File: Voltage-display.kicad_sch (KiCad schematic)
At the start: 17 parts, among them J1 Conn_01x02, J2 Conn_01x02, U1 AMC1311BQDWVQ1, U2 R05CT05S-R

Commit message: Assigned Footprints to the components
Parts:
- U1: footprint DWV8_TEX -> ul_AMC1311BQDWVQ1_footprints:DWV8_TEX
- U2: footprint SMD_16_10.3X7.5X2.6_RCP -> R05CT055_R_footprints:SMD_16_10.3X7.5X2.6_RCP
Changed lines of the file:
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@@
 			)
 		)
-		(property "Footprint" "DWV8_TEX"
+		(property "Footprint" "ul_AMC1311BQDWVQ1_footprints:DWV8_TEX"
 			(at 102.87 125.73 0)
 			(hide yes)
@@
 			)
 		)
-		(property "Footprint" "SMD_16_10.3X7.5X2.6_RCP"
+		(property "Footprint" "R05CT055_R_footprints:SMD_16_10.3X7.5X2.6_RCP"
 			(at 97.79 36.83 0)
 			(hide yes)

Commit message: Assigned more footprints on caps and resistors
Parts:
- C1, C2, C3, C4, C5, C6, C8: footprint (none) -> Capacitor_SMD:C_0805_2012Metric_Pad1.18x1.45mm_HandSolder
- C7, C9: footprint (none) -> Capacitor_SMD:C_1206_3216Metric_Pad1.33x1.80mm_HandSolder
- R1: footprint Resistor_THT:R_Array_SIP6 -> Resistor_SMD:R_1206_3216Metric_Pad1.30x1.75mm_HandSolder
- R2, R3, R4: footprint (none) -> Resistor_SMD:R_1206_3216Metric_Pad1.30x1.75mm_HandSolder
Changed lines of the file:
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@@
 			)
 		)
-		(property "Footprint" ""
+		(property "Footprint" "Capacitor_SMD:C_1206_3216Metric_Pad1.33x1.80mm_HandSolder"
 			(at 187.6552 86.36 0)
 			(hide yes)
@@
 			)
 		)
-		(property "Footprint" ""
+		(property "Footprint" "Capacitor_SMD:C_0805_2012Metric_Pad1.18x1.45mm_HandSolder"
 			(at 171.1452 86.36 0)
 			(hide yes)
@@
 			)
 		)
-		(property "Footprint" ""
+		(property "Footprint" "Resistor_SMD:R_1206_3216Metric_Pad1.30x1.75mm_HandSolder"
 			(at 20.32 44.45 0)
 			(hide yes)
@@
 			)
 		)
-		(property "Footprint" ""
+		(property "Footprint" "Capacitor_SMD:C_0805_2012Metric_Pad1.18x1.45mm_HandSolder"
 			(at 220.6752 34.29 0)
 			(hide yes)
@@
 			)
 		)
-		(property "Footprint" ""
+		(property "Footprint" "Resistor_SMD:R_1206_3216Metric_Pad1.30x1.75mm_HandSolder"
 			(at 20.32 66.04 0)
 			(hide yes)
@@
 			)
 		)
-		(property "Footprint" ""
+		(property "Footprint" "Capacitor_SMD:C_0805_2012Metric_Pad1.18x1.45mm_HandSolder"
 			(at 174.9552 34.29 0)
 			(hide yes)
@@
 			)
 		)
-		(property "Footprint" "Resistor_THT:R_Array_SIP6"
+		(property "Footprint" "Resistor_SMD:R_1206_3216Metric_Pad1.30x1.75mm_HandSolder"
 			(at 20.32 34.29 0)
 			(hide yes)
@@
 			)
 		)
-		(property "Footprint" ""
+		(property "Footprint" "Capacitor_SMD:C_1206_3216Metric_Pad1.33x1.80mm_HandSolder"
 			(at 220.6752 85.09 0)
 			(hide yes)
@@
 			)
 		)
-		(property "Footprint" ""
+		(property "Footprint" "Capacitor_SMD:C_0805_2012Metric_Pad1.18x1.45mm_HandSolder"
 			(at 204.1652 85.09 0)
 			(hide yes)
@@
 			)
 		)
-		(property "Footprint" ""
+		(property "Footprint" "Resistor_SMD:R_1206_3216Metric_Pad1.30x1.75mm_HandSolder"
 			(at 20.32 54.61 0)
 			(hide yes)
@@
 			)
 		)
-		(property "Footprint" ""
+		(property "Footprint" "Capacitor_SMD:C_0805_2012Metric_Pad1.18x1.45mm_HandSolder"
 			(at 36.5252 72.39 0)
 			(hide yes)
@@
 			)
 		)
-		(property "Footprint" ""
+		(property "Footprint" "Capacitor_SMD:C_0805_2012Metric_Pad1.18x1.45mm_HandSolder"
 			(at 191.4652 34.29 0)
 			(hide yes)
@@
 			)
 		)
-		(property "Footprint" ""
+		(property "Footprint" "Capacitor_SMD:C_0805_2012Metric_Pad1.18x1.45mm_HandSolder"
 			(at 204.1652 34.29 0)
 			(hide yes)

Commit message: Add KiCad project
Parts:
- J1, J2: footprint (none) -> Connector:Banana_Jack_2Pin
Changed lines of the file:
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@@
 			)
 		)
-		(property "Footprint" ""
+		(property "Footprint" "Connector:Banana_Jack_2Pin"
 			(at 53.34 27.94 0)
 			(hide yes)
@@
 			)
 		)
-		(property "Footprint" ""
+		(property "Footprint" "Connector:Banana_Jack_2Pin"
 			(at 38.1 114.3 0)
 			(hide yes)

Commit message: Update KiCad PCB
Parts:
- J1, J2: footprint Connector:Banana_Jack_2Pin -> TerminalBlock_Phoenix:TerminalBlock_Phoenix_PTSM-0,5-2-2,5-V-SMD_1x02-1MP_P2.50mm_Vertical
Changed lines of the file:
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@@
 			)
 		)
-		(property "Footprint" "Connector:Banana_Jack_2Pin"
+		(property "Footprint" "TerminalBlock_Phoenix:TerminalBlock_Phoenix_PTSM-0,5-2-2,5-V-SMD_1x02-1MP_P2.50mm_Vertical"
 			(at 53.34 27.94 0)
 			(hide yes)
@@
 			)
 		)
-		(property "Footprint" "Connector:Banana_Jack_2Pin"
+		(property "Footprint" "TerminalBlock_Phoenix:TerminalBlock_Phoenix_PTSM-0,5-2-2,5-V-SMD_1x02-1MP_P2.50mm_Vertical"
 			(at 38.1 114.3 0)
 			(hide yes)

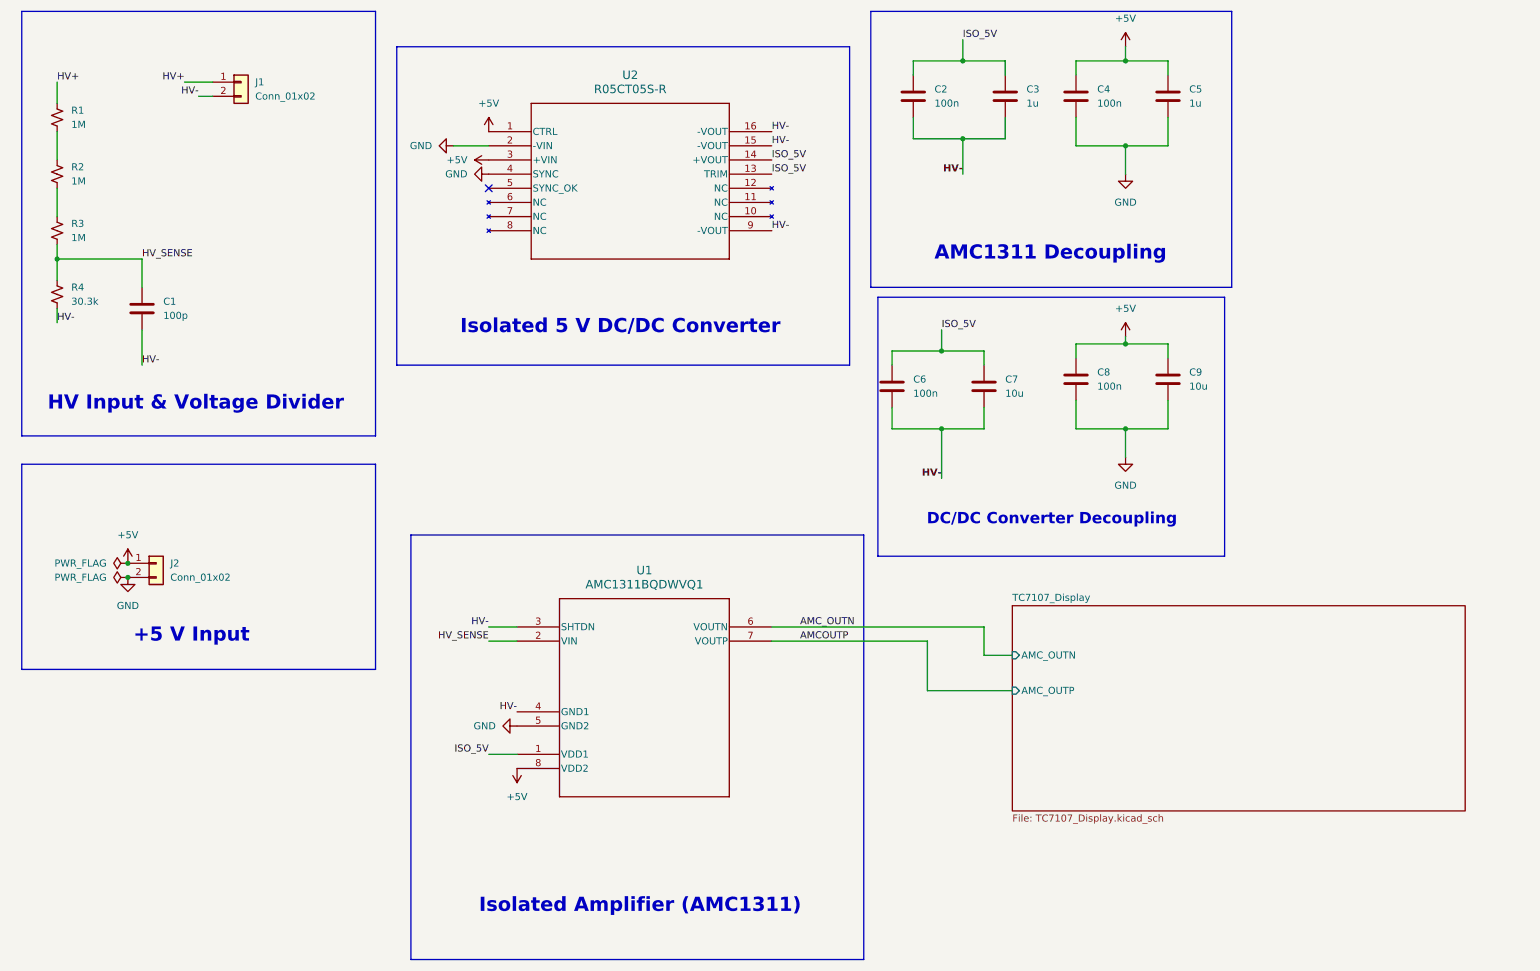
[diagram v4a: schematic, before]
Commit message: Updated with Safety/Protection features
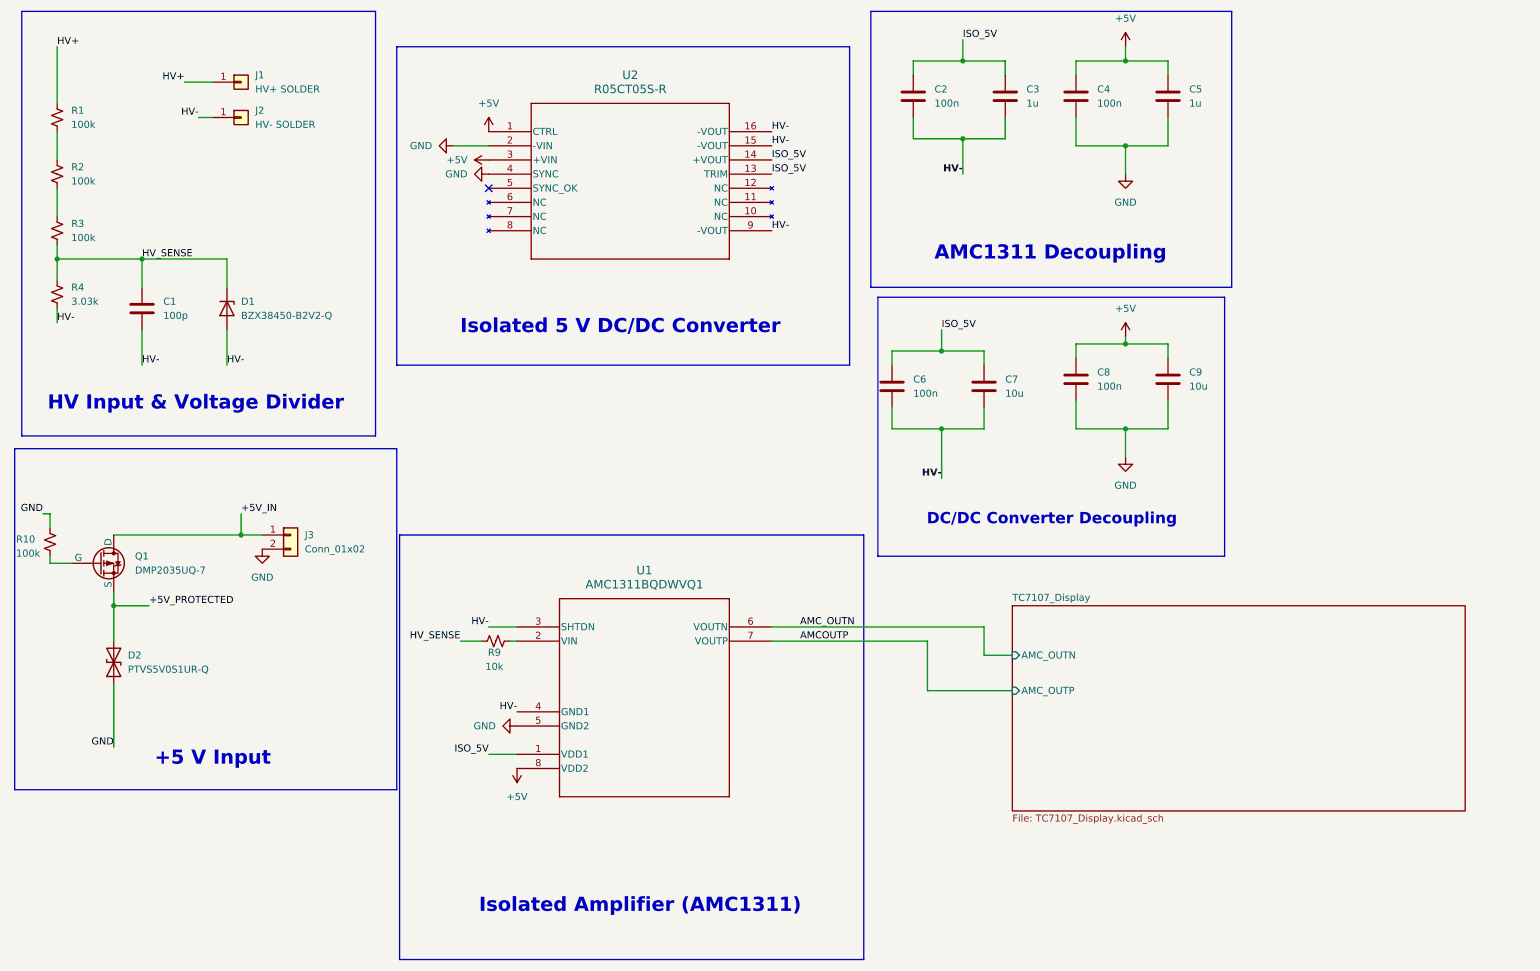
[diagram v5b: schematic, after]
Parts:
- removed J1: Conn_01x02, TerminalBlock_Phoenix:TerminalBlock_Phoenix_PTSM-0,5-2-2,5-V-SMD_1x02-1MP_P2.50mm_Vertical, symbol Connector_Generic:Conn_01x02
- added D1: BZX38450-B2V2-Q, Diode_SMD:D_SOD-323_HandSoldering, symbol Device:D_Zener
- added D2: PTVS5V0S1UR-Q, Voltage_Display_Footprints:SOD123W, symbol Device:D_TVS
- added J1: HV+ SOLDER, Connector_Wire:SolderWire-0.5sqmm_1x01_D0.9mm_OD2.1mm_Relief, symbol Connector_Generic:Conn_01x01
- added J2: HV- SOLDER, Connector_Wire:SolderWire-0.5sqmm_1x01_D0.9mm_OD2.1mm_Relief, symbol Connector_Generic:Conn_01x01
- added Q1: DMP2035UQ-7, Voltage_Display_Footprints:SOT96P240X115-3N, symbol Simulation_SPICE:PMOS
- added R10: 100k, Resistor_SMD:R_1206_3216Metric_Pad1.30x1.75mm_HandSolder, symbol Device:R_Small_US
- added R9: 10k, Resistor_SMD:R_1206_3216Metric_Pad1.30x1.75mm_HandSolder, symbol Device:R_Small_US
- J3: renamed from J2; footprint TerminalBlock_Phoenix:TerminalBlock_Phoenix_PTSM-0,5-2-2,5-V-SMD_1x02-1MP_P2.50mm_Vertical -> Connector_PinHeader_2.54mm:PinHeader_1x02_P2.54mm_Vertical
- R1, R2, R3: value 1M -> 100k
- R4: value 30.3k -> 3.03k
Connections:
- net +5V: no longer J3.1 (Pin_1)
- net GND: now also D2.1 (A1), R10.1
- net HV+: now also J1.1 (Pin_1)
- net HV-: now also D1.2 (A), J2.1 (Pin_1)
- net HV_SENSE: now also D1.1 (K), R9.1; no longer U1.2 (VIN)
- new net: R9.2, U1.2 (VIN)
- new net: Q1.2 (G), R10.2
- new net +5V_IN: J3.1 (Pin_1), Q1.1 (D)
- new net +5V_PROTECTED: D2.2 (A2), Q1.3 (S)
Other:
- moved on the sheet: J3

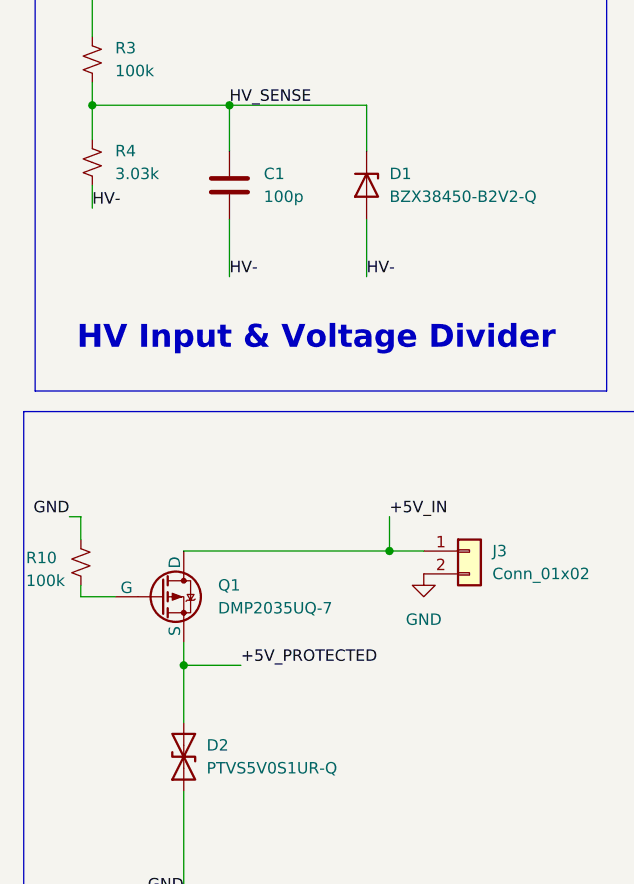
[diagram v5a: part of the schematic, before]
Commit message: Added the switch for the votlage display
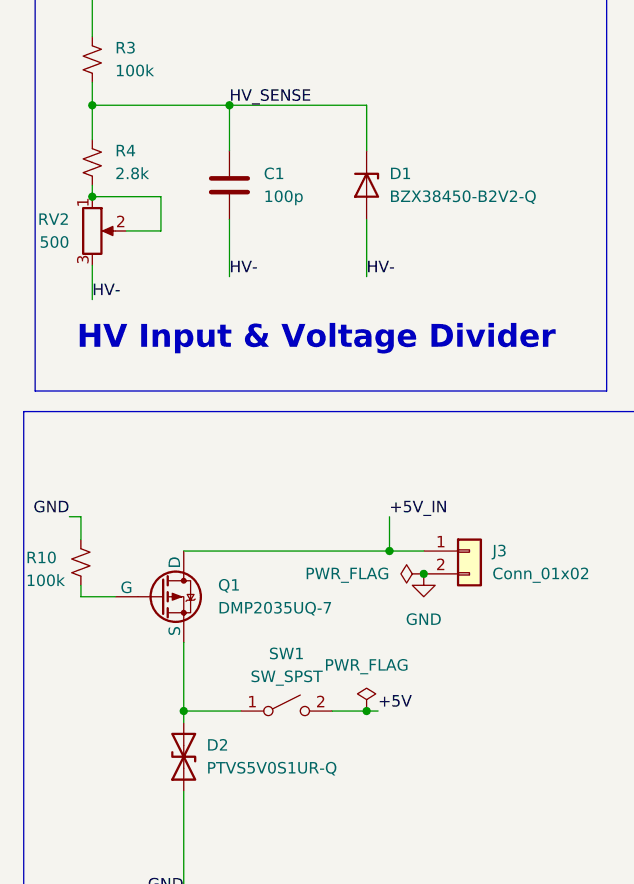
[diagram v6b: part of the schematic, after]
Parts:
- added RV2: 500, Potentiometer_THT:Potentiometer_Bourns_3296W_Vertical, symbol Device:R_Potentiometer
- added SW1: SW_SPST, symbol Switch:SW_SPST
- R4: value 3.03k -> 2.8k
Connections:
- net +5V: now also SW1.2 (B)
- net HV-: now also RV2.3; no longer R4.2
- net +5V_PROTECTED: no longer names the net of D2.2 (A2), Q1.3 (S)
- net +5V_PROTECTED: now also SW1.1 (A)
- new net: R4.2, RV2.1, RV2.2

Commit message: Update files
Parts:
- removed J1: HV+ SOLDER, Connector_Wire:SolderWire-0.5sqmm_1x01_D0.9mm_OD2.1mm_Relief, symbol Connector_Generic:Conn_01x01
- removed J2: HV- SOLDER, Connector_Wire:SolderWire-0.5sqmm_1x01_D0.9mm_OD2.1mm_Relief, symbol Connector_Generic:Conn_01x01
- removed RV2: 500, Potentiometer_THT:Potentiometer_Bourns_3296W_Vertical, symbol Device:R_Potentiometer
- added J1: Conn_01x02, Connector_PinHeader_2.54mm:PinHeader_1x02_P2.54mm_Vertical, symbol Connector_Generic:Conn_01x02
- added R11: 300, Resistor_SMD:R_1206_3216Metric_Pad1.30x1.75mm_HandSolder, symbol Device:R_Small_US
- D1: value BZX38450-B2V2-Q -> BZX38450-C2V2-QX
- R4: value 2.8k -> 3k
- renumbered J3 to J2
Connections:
- net HV+: now also J1.1 (Pin_1)
- net HV-: now also J1.2 (Pin_2), R11.2
- net at R4.2: now also R11.1
